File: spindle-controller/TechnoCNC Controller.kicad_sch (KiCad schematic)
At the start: 2 parts, among them J25 GX12-2, K1 Relay_SPDT

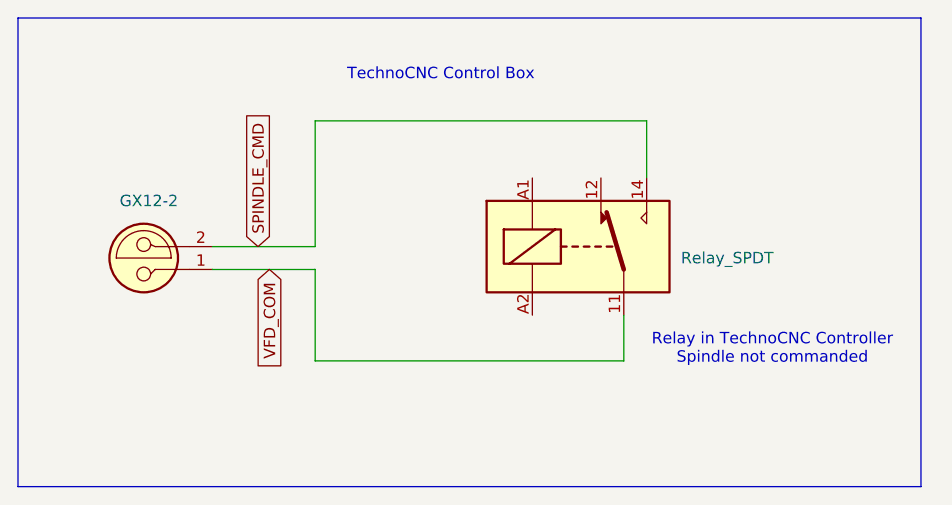
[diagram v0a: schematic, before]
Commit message: updated connectors
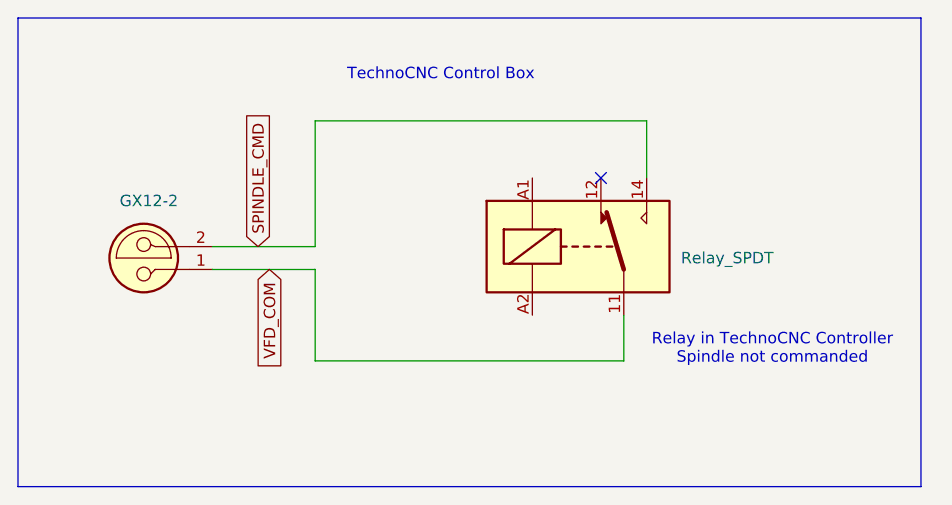
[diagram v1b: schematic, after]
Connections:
- no-connect marks 0 -> 1
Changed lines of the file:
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@@
 		)
+	)
+	(no_connect
+		(at 161.29 82.55)
 	)
 	(wire
